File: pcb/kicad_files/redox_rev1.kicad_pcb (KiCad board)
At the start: 2 copper layers, 162.2 x 126.5 mm, 90 parts, among them K0 KEYSW, K1 KEYSW, K10 KEYSW, K11 KEYSW, K12 KEYSW, K13 KEYSW, K14 KEYSW, K15 KEYSW, K16 KEYSW, K2 KEYSW, K20 KEYSW, K21 KEYSW, K22 KEYSW, K23 KEYSW, K24 KEYSW, K25 KEYSW, K26 KEYSW, K3 KEYSW, K30 KEYSW, K31 KEYSW, K32 KEYSW, K33 KEYSW, K34 KEYSW, K35 KEYSW, K36 KEYSW, K4 KEYSW, K40 KEYSW, K41 KEYSW, K42 KEYSW, K43 KEYSW, K44 KEYSW, K45 KEYSW, K46 KEYSW, K5 KEYSW, K6 KEYSW, U1 ProMicro

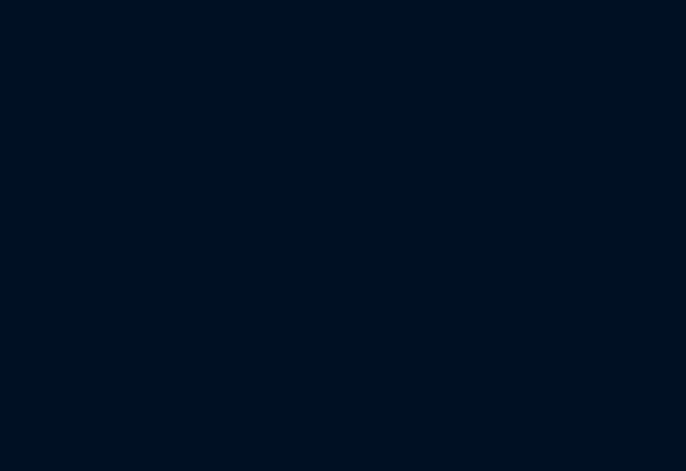
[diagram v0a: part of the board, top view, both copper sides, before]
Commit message: Added oled
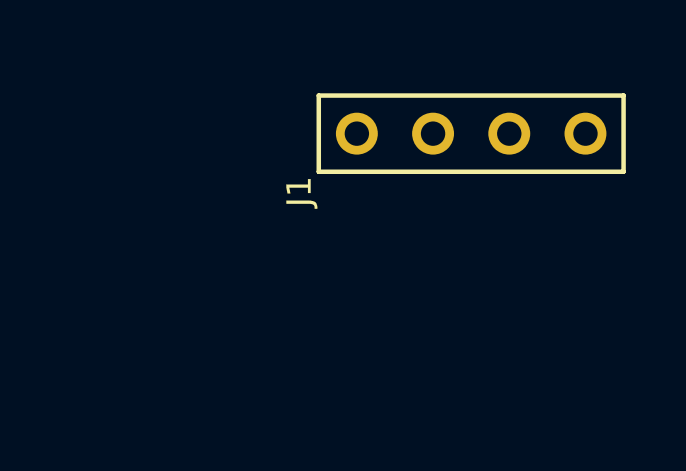
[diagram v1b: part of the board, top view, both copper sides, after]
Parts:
- added J1: OLED-Lily58-cache, Lily58_Pro-footprint:OLED_4Pin, F.Cu at (266.3, 51.0)
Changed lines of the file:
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@@
     (tracks 826)
     (zones 0)
-    (modules 90)
+    (modules 91)
     (nets 58)
   )
@@
   )
   (layers
-    (0 F.Cu signal hide)
+    (0 F.Cu signal)
     (31 B.Cu signal hide)
     (32 B.Adhes user hide)
@@
     (36 B.SilkS user)
     (37 F.SilkS user hide)
-    (38 B.Mask user hide)
-    (39 F.Mask user hide)
-    (40 Dwgs.User user hide)
-    (41 Cmts.User user hide)
-    (42 Eco1.User user hide)
-    (43 Eco2.User user hide)
-    (44 Edge.Cuts user hide)
-    (45 Margin user hide)
-    (46 B.CrtYd user hide)
-    (47 F.CrtYd user hide)
-    (48 B.Fab user hide)
-    (49 F.Fab user hide)
+    (38 B.Mask user)
+    (39 F.Mask user)
+    (40 Dwgs.User user)
+    (41 Cmts.User user)
+    (42 Eco1.User user)
+    (43 Eco2.User user)
+    (44 Edge.Cuts user)
+    (45 Margin user)
+    (46 B.CrtYd user)
+    (47 F.CrtYd user)
+    (48 B.Fab user)
+    (49 F.Fab user)
   )
   (setup
@@
       (xy -9.943822 1.795852)) (layer B.SilkS) (width 0.01))
   )
+  (module Lily58_Pro-footprint:OLED_4Pin (layer F.Cu)
+    (at 266.3 50.95)
+    (descr "Connecteur 6 pins")
+    (tags "CONN DEV")
+    (fp_text reference J1 (at -1.915 1.93 90) (layer F.SilkS)
+      (effects (font (size 0.8128 0.8128) (thickness 0.15)))
+    )
+    (fp_text value OLED-Lily58-cache (at 3.81 1.27) (layer F.SilkS) hide
+      (effects (font (size 0.8128 0.8128) (thickness 0.15)))
+    )
+    (fp_line (start -1.27 -1.27) (end 8.89 -1.27) (layer B.SilkS) (width 0.15))
+    (fp_line (start 8.89 -1.27) (end 8.89 1.27) (layer B.SilkS) (width 0.15))
+    (fp_line (start 8.89 1.27) (end -1.27 1.27) (layer B.SilkS) (width 0.15))
+    (fp_line (start -1.27 1.27) (end -1.27 -1.27) (layer B.SilkS) (width 0.15))
+    (fp_line (start -1.27 1.27) (end 8.89 1.27) (layer F.SilkS) (width 0.15))
+    (fp_line (start -1.27 -1.27) (end 8.89 -1.27) (layer F.SilkS) (width 0.15))
+    (fp_line (start 8.89 -1.27) (end 8.89 1.27) (layer F.SilkS) (width 0.15))
+    (fp_line (start -1.27 1.27) (end -1.27 -1.27) (layer F.SilkS) (width 0.15))
+    (pad 1 thru_hole circle (at 0 0) (size 1.397 1.397) (drill 0.8128) (layers *.Cu *.Mask F.SilkS)
+      (net 52 GND))
+    (pad 2 thru_hole circle (at 2.54 0) (size 1.397 1.397) (drill 0.8128) (layers *.Cu *.Mask F.SilkS)
+      (net 48 VCC))
+    (pad 3 thru_hole circle (at 5.08 0) (size 1.397 1.397) (drill 0.8128) (layers *.Cu *.Mask F.SilkS)
+      (net 50 SCL))
+    (pad 4 thru_hole circle (at 7.62 0) (size 1.397 1.397) (drill 0.8128) (layers *.Cu *.Mask F.SilkS)
+      (net 49 SDA))
+  )
   (gr_text "designed by Mattia Dal Ben (modified by Ian Lim Hee Lai)\n" (at 81.915 94.488 90) (layer F.SilkS)

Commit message: update netsat
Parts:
- moved J1 20.6 mm to (246.6, 56.9)
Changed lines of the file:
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@@
   )
   (layers
-    (0 F.Cu signal)
+    (0 F.Cu signal hide)
     (31 B.Cu signal hide)
     (32 B.Adhes user hide)
@@
     (34 B.Paste user hide)
     (35 F.Paste user hide)
-    (36 B.SilkS user)
+    (36 B.SilkS user hide)
     (37 F.SilkS user hide)
-    (38 B.Mask user)
-    (39 F.Mask user)
-    (40 Dwgs.User user)
-    (41 Cmts.User user)
-    (42 Eco1.User user)
-    (43 Eco2.User user)
-    (44 Edge.Cuts user)
-    (45 Margin user)
-    (46 B.CrtYd user)
-    (47 F.CrtYd user)
-    (48 B.Fab user)
-    (49 F.Fab user)
+    (38 B.Mask user hide)
+    (39 F.Mask user hide)
+    (40 Dwgs.User user hide)
+    (41 Cmts.User user hide)
+    (42 Eco1.User user hide)
+    (43 Eco2.User user hide)
+    (44 Edge.Cuts user hide)
+    (45 Margin user hide)
+    (46 B.CrtYd user hide)
+    (47 F.CrtYd user hide)
+    (48 B.Fab user hide)
+    (49 F.Fab user hide)
   )
   (setup
@@
   )
   (module Lily58_Pro-footprint:OLED_4Pin (layer F.Cu)
-    (at 266.3 50.95)
+    (at 246.575 56.875)
     (descr "Connecteur 6 pins")
     (tags "CONN DEV")

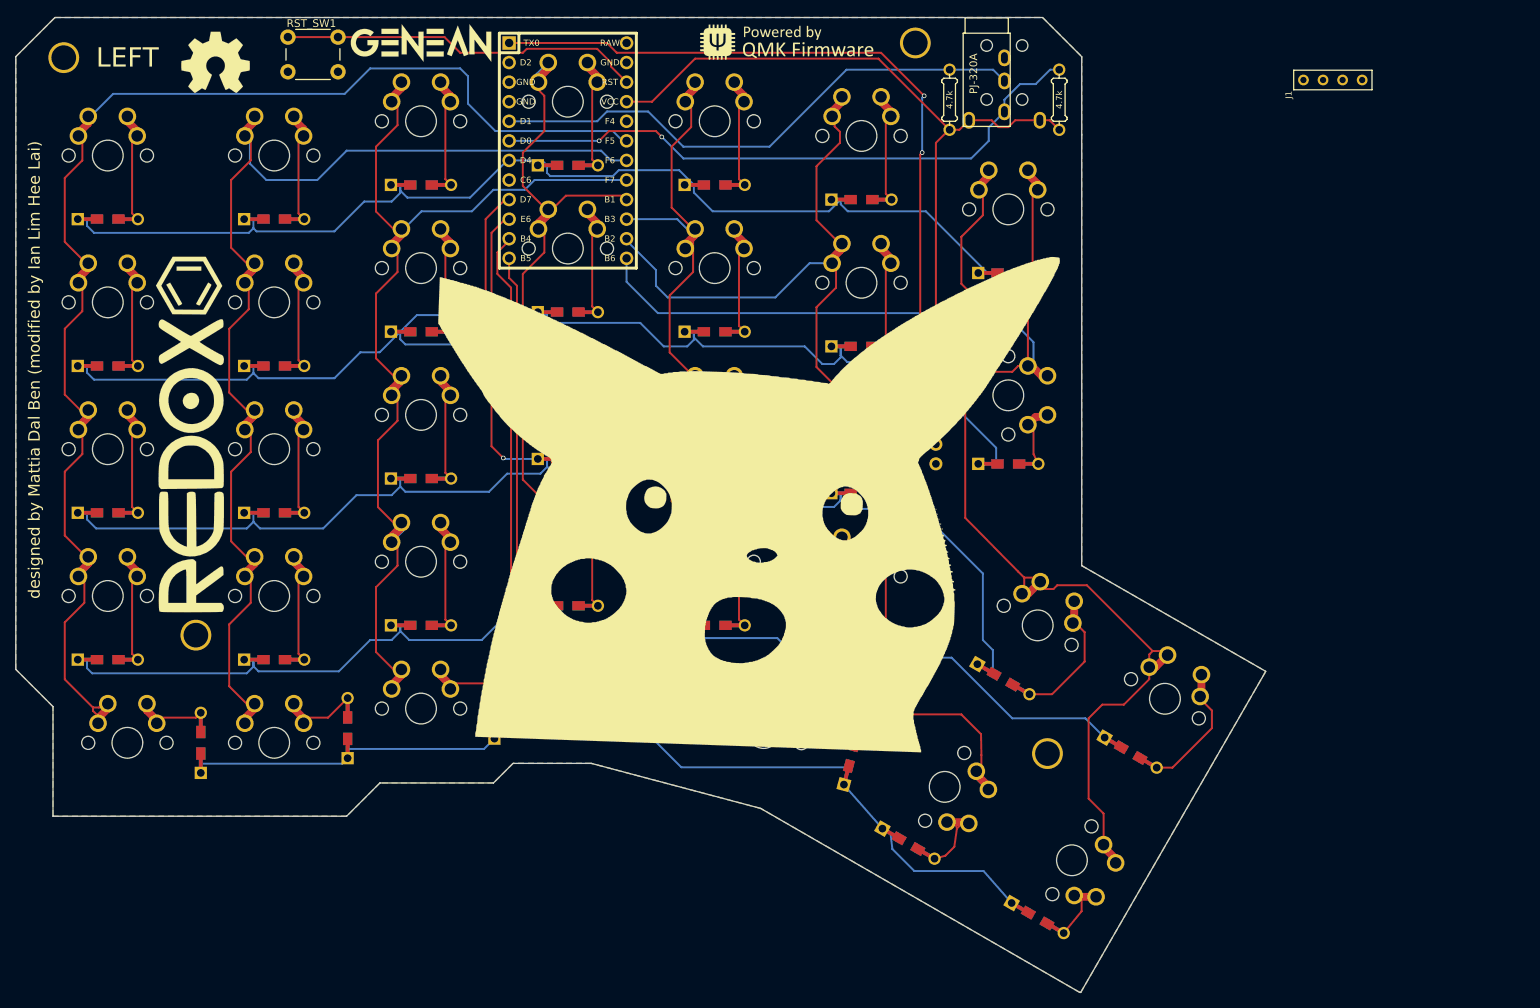
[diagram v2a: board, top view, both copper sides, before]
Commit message: Completed pcb routing
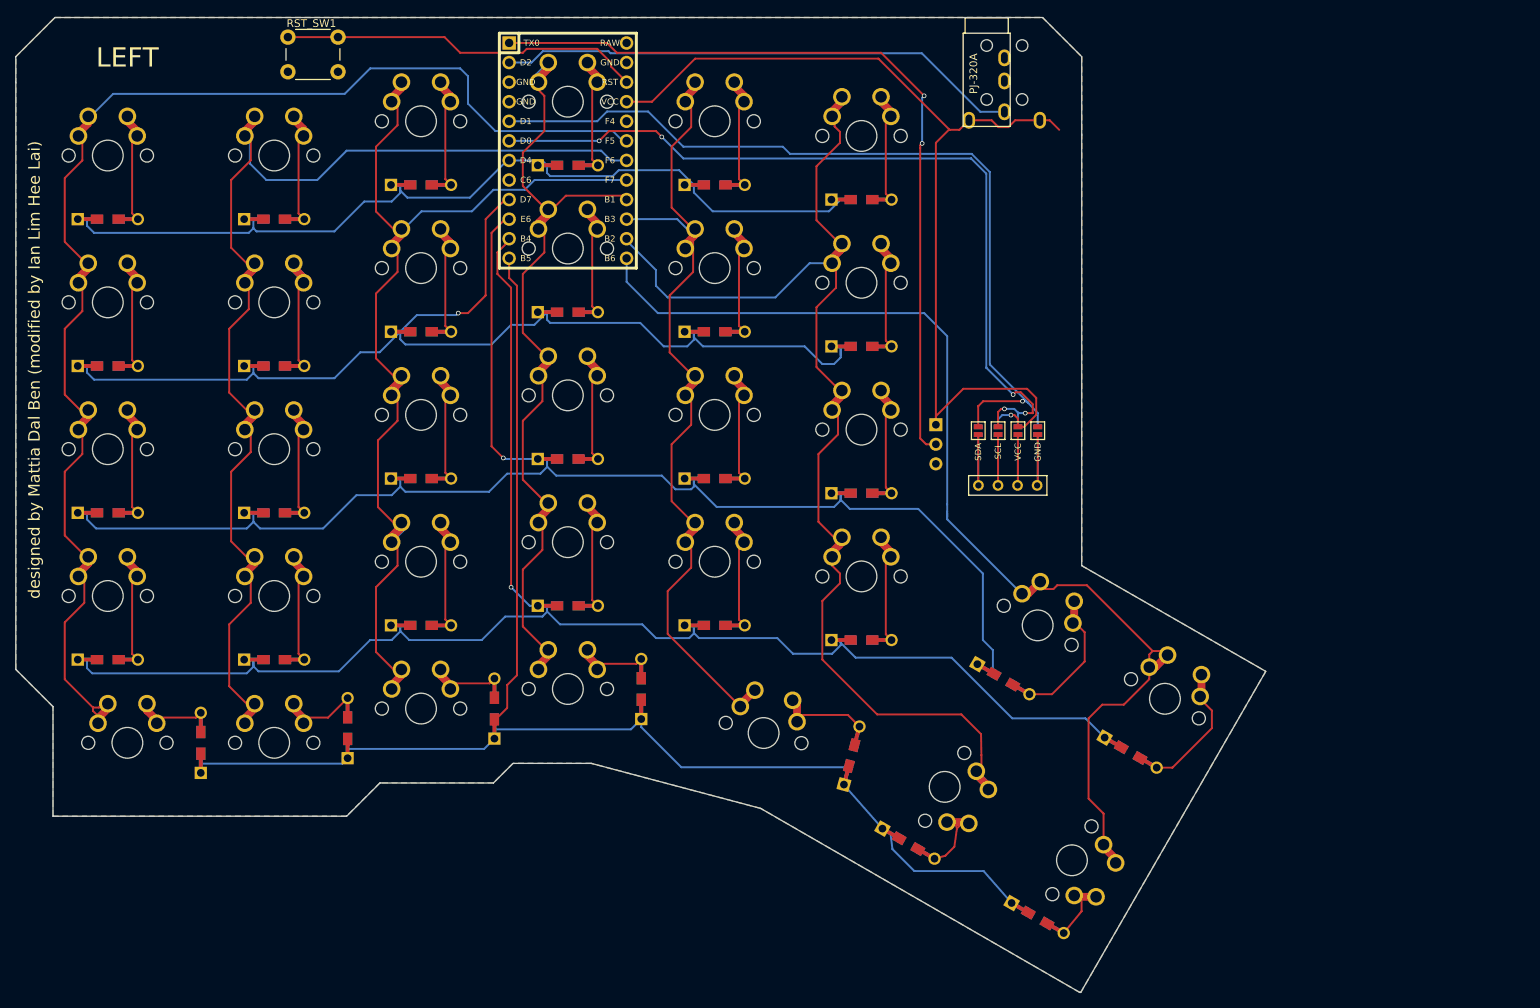
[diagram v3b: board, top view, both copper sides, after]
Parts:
- removed D16, D6: D, Keebio-Parts:Diode-dual
- removed G***: LOGO, keyswitches:pika
- removed G***: LOGO, keyswitches:pika_reflected
- removed G*** (x2): LOGO, redox_footprints:genean-logo-fp
- removed G*** (x2): LOGO, myparts:redox-logo
- removed G*** (x2): LOGO, myparts:qmk-badge
- removed HOLE_M3 (x4): VAL**, keyboard_parts:HOLE_M3
- removed K16, K6: KEYSW, keyswitches:SW_MX_reversible
- removed R1, R2: 4.7k, Keebio-Parts:Resistor-Compact
- removed REF*** (x2): OSHW-Logo2_14.6x12mm_SilkScreen, Symbols:OSHW-Symbol_8.9x8mm_SilkScreen
- added JP1: SDA, Lily58_Pro-footprint:Jumper, F.Cu at (204.4, 102.4)
- added JP2: SCL, Lily58_Pro-footprint:Jumper, F.Cu at (206.9, 102.4)
- added JP3: VCC, Lily58_Pro-footprint:Jumper, F.Cu at (209.5, 102.4)
- added JP4: GND, Lily58_Pro-footprint:Jumper, F.Cu at (212.1, 102.4)
- added JP5: GND, Lily58_Pro-footprint:Jumper, B.Cu at (204.4, 102.4)
- added JP6: VCC, Lily58_Pro-footprint:Jumper, B.Cu at (206.9, 102.4)
- added JP7: SCL, Lily58_Pro-footprint:Jumper, B.Cu at (209.5, 102.4)
- added JP8: SDA, Lily58_Pro-footprint:Jumper, B.Cu at (212.1, 102.4)
- moved J1 67.4 mm to (204.4, 109.5)
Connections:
- J1 pad 1: GND -> Net-(J1-Pad1)
- J1 pad 2: VCC -> Net-(J1-Pad2)
- J1 pad 3: SCL -> Net-(J1-Pad3)
- J1 pad 4: SDA -> Net-(J1-Pad4)
- TRRS1 pad 2: SCL -> serial
- TRRS1 pad 3: SDA -> Net-(TRRS1-Pad3)
- U1 pad 2: Net-(U1-Pad2) -> serial
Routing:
- net serial: track 0.00 -> 68.1 mm
- net col6: track 203.5 -> 146.8 mm
- net SDA: track 71.4 -> 111.2 mm, vias 0 -> 1
- net SCL: track 80.1 -> 108.0 mm, vias 2 -> 5
- net row1: track 169.3 -> 142.1 mm
- net VCC: track 103.1 -> 129.4 mm, vias 0 -> 1
- net row0: track 135.3 -> 112.0 mm
- net Net-(D6-Pad2): track 14.9 -> 0.00 mm
- net Net-(J1-Pad4): track 0.00 -> 13.3 mm
- net Net-(J1-Pad3): track 0.00 -> 13.2 mm
- net Net-(J1-Pad1): track 0.00 -> 13.2 mm
- net Net-(J1-Pad2): track 0.00 -> 13.2 mm
- net Net-(D16-Pad2): track 9.20 -> 0.00 mm
